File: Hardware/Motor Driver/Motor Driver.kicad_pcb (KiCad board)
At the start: 2 copper layers, 65 x 85 mm, 10 parts, among them J1 Conn_01x02, J2 Conn_01x02, J3 Conn_01x04, J4 Conn_01x04, J5 Conn_01x06, J6 Conn_01x06, J7 Conn_01x02

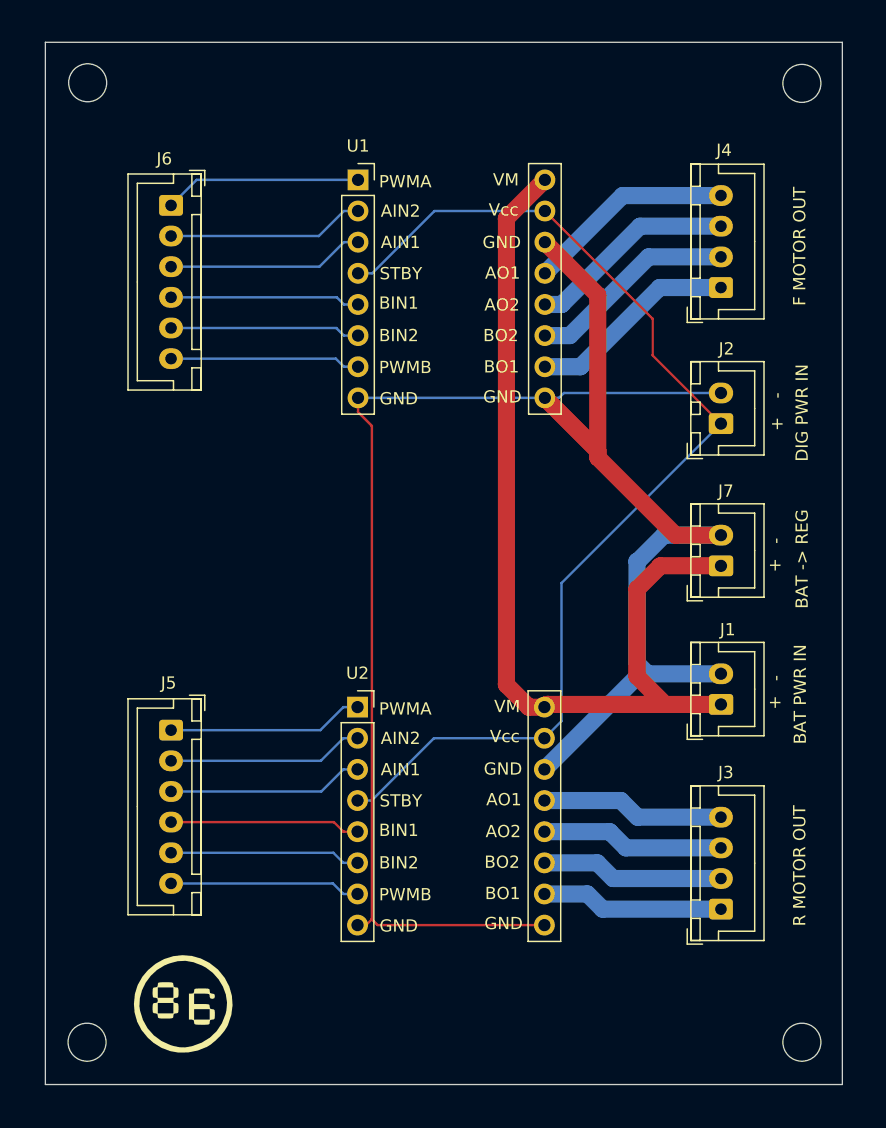
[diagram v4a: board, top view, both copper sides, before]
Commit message: Added copper fill to both sides of the board.
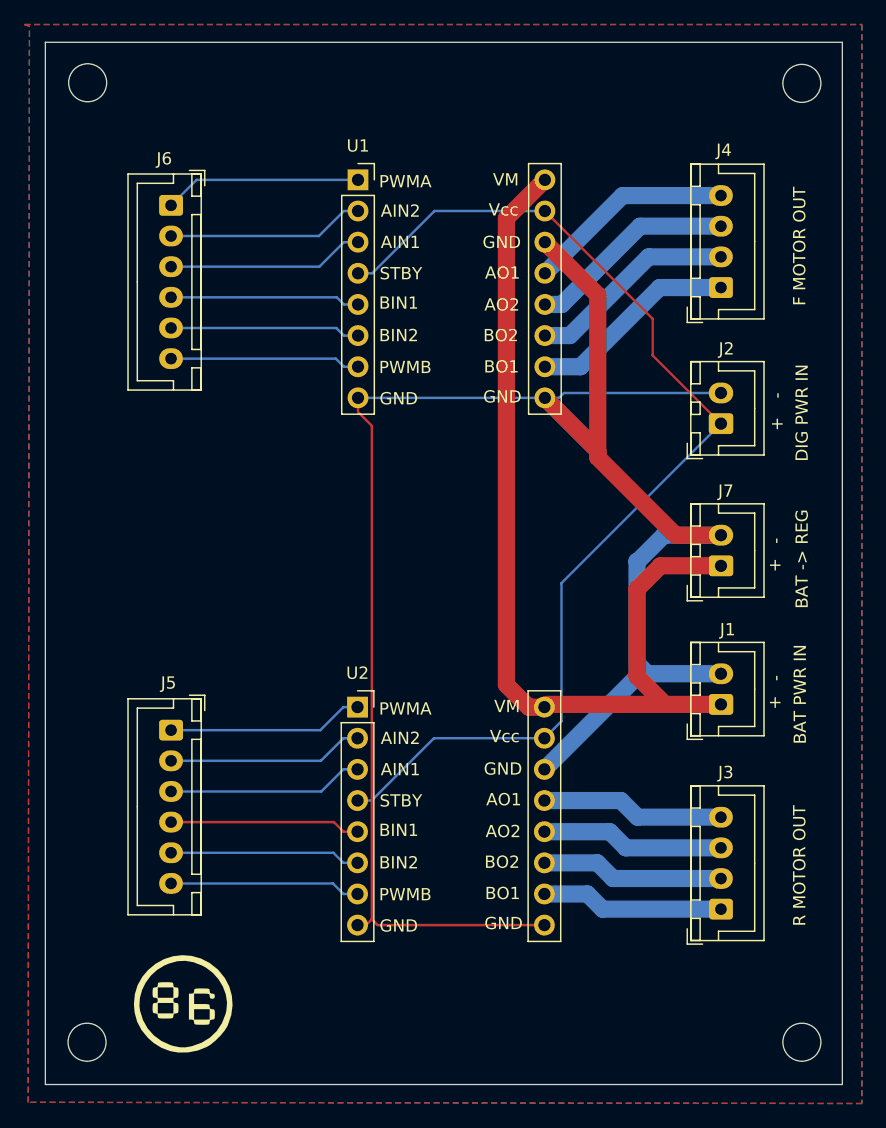
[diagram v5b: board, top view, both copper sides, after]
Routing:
- added copper zone on B.Cu, net (none)
- added copper zone on F.Cu, net (none)
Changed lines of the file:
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@@
 		(net 23)
 	)
+	(zone
+		(net 0)
+		(net_name "")
+		(layers "F&B.Cu")
+		(hatch edge 0.5)
+		(connect_pads
+			(clearance 0.5)
+		)
+		(min_thickness 0.25)
+		(filled_areas_thickness no)
+		(fill yes
+			(thermal_gap 0.5)
+			(thermal_bridge_width 0.5)
+			(island_removal_mode 1)
+			(island_area_min 10)
+		)
+		(polygon
+			(pts
+				(xy 98.3 48.55) (xy 166.6 48.55) (xy 166.6 136.55) (xy 98.6 136.45) (xy 98.7 48.7)
+			)
+		)
+	)
 )
